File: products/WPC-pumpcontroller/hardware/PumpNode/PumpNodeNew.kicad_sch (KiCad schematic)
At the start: 37 parts, among them J1 Conn_IN, J2 Conn_Coaxial_Small, J3 PWR_CONN, J4 Relay_CONN, K1 Cube_Relay, U1 ULN2003, U13 AMS1117-5.0, U5 ESP32 30 Pin CP2102 Developme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, U7 ISC-SX1262-B, U8 AP2112K-3.3

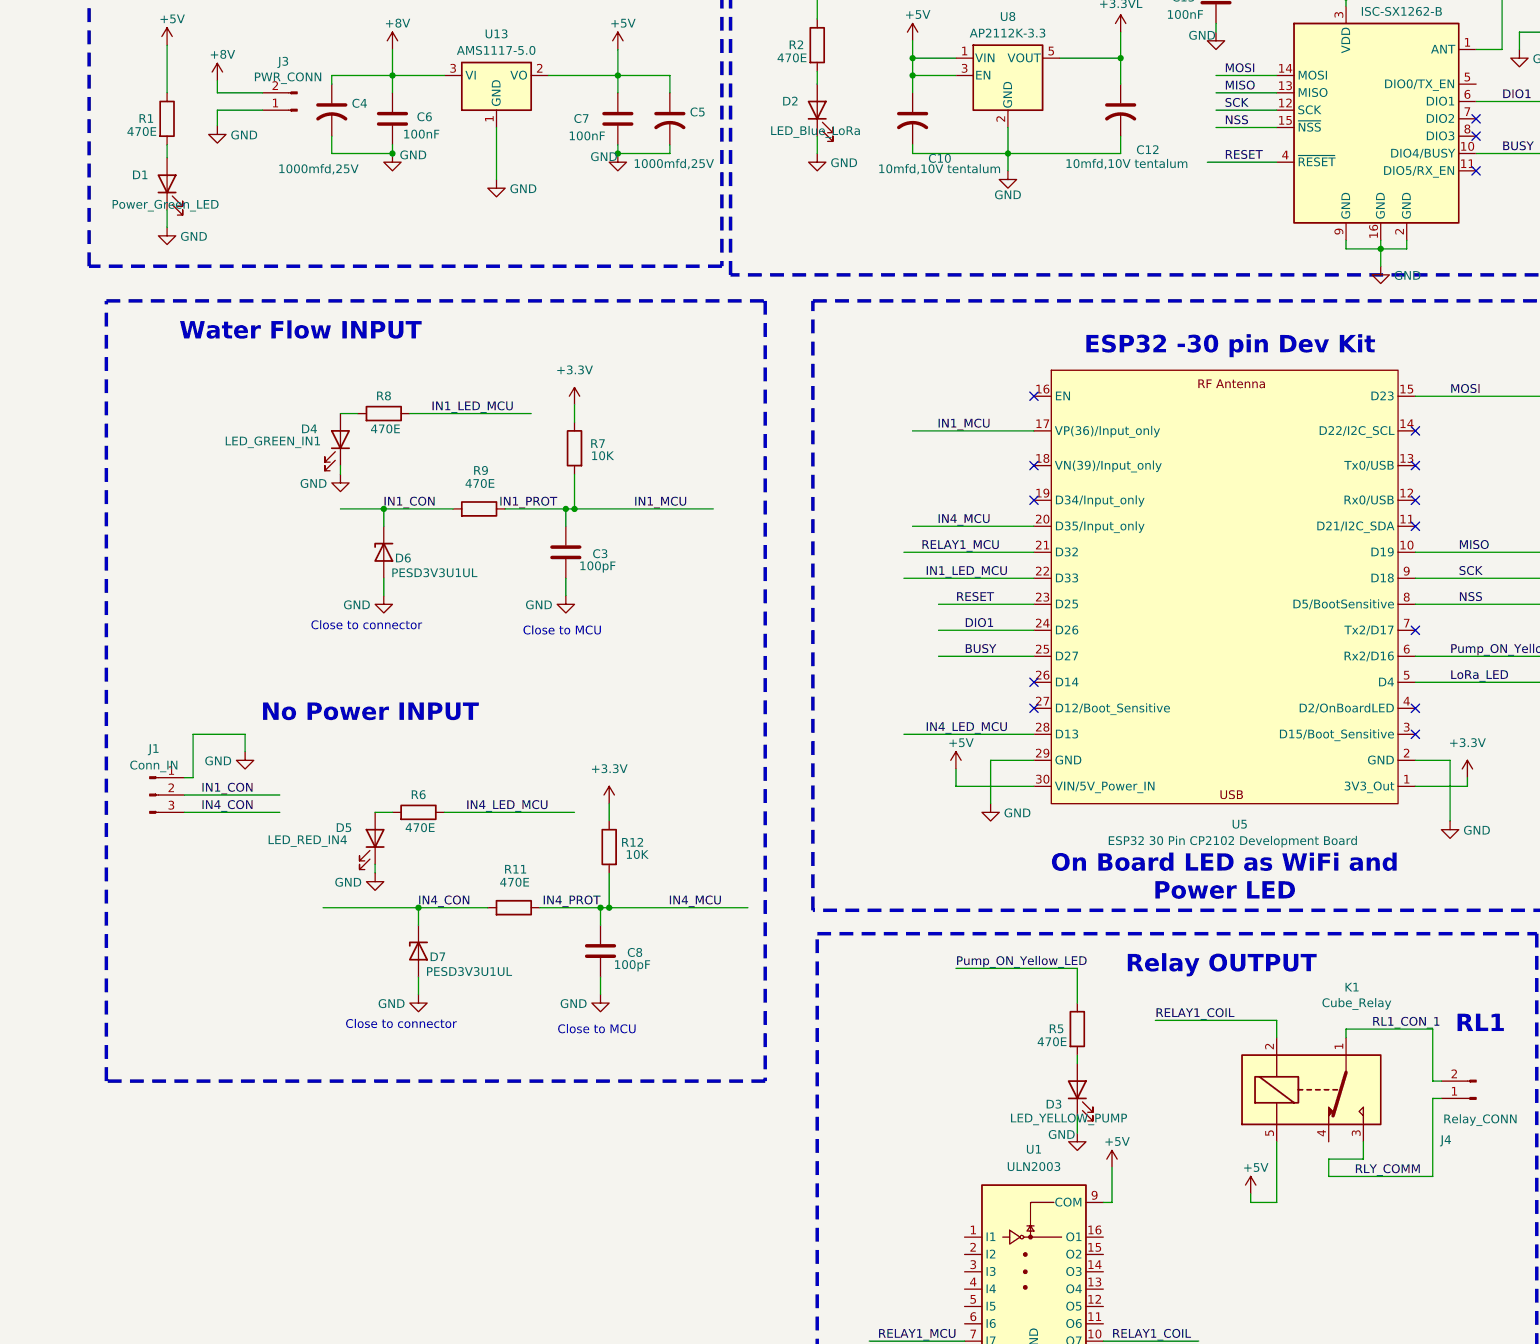
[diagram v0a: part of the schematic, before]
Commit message: WPC: PumpNode + WPC board updates, add 2x panel and Gerber exports
- Update PumpNode and WPC KiCad PCB/schematic/project-local files
- Add WPC-panel2x (2-up panelized PumpNode layout) KiCad project
- Add Gerber/drill export sets for PumpNode and the 2x panel

Co-Authored-By: Claude Sonnet 5 <noreply@anthropic.com>
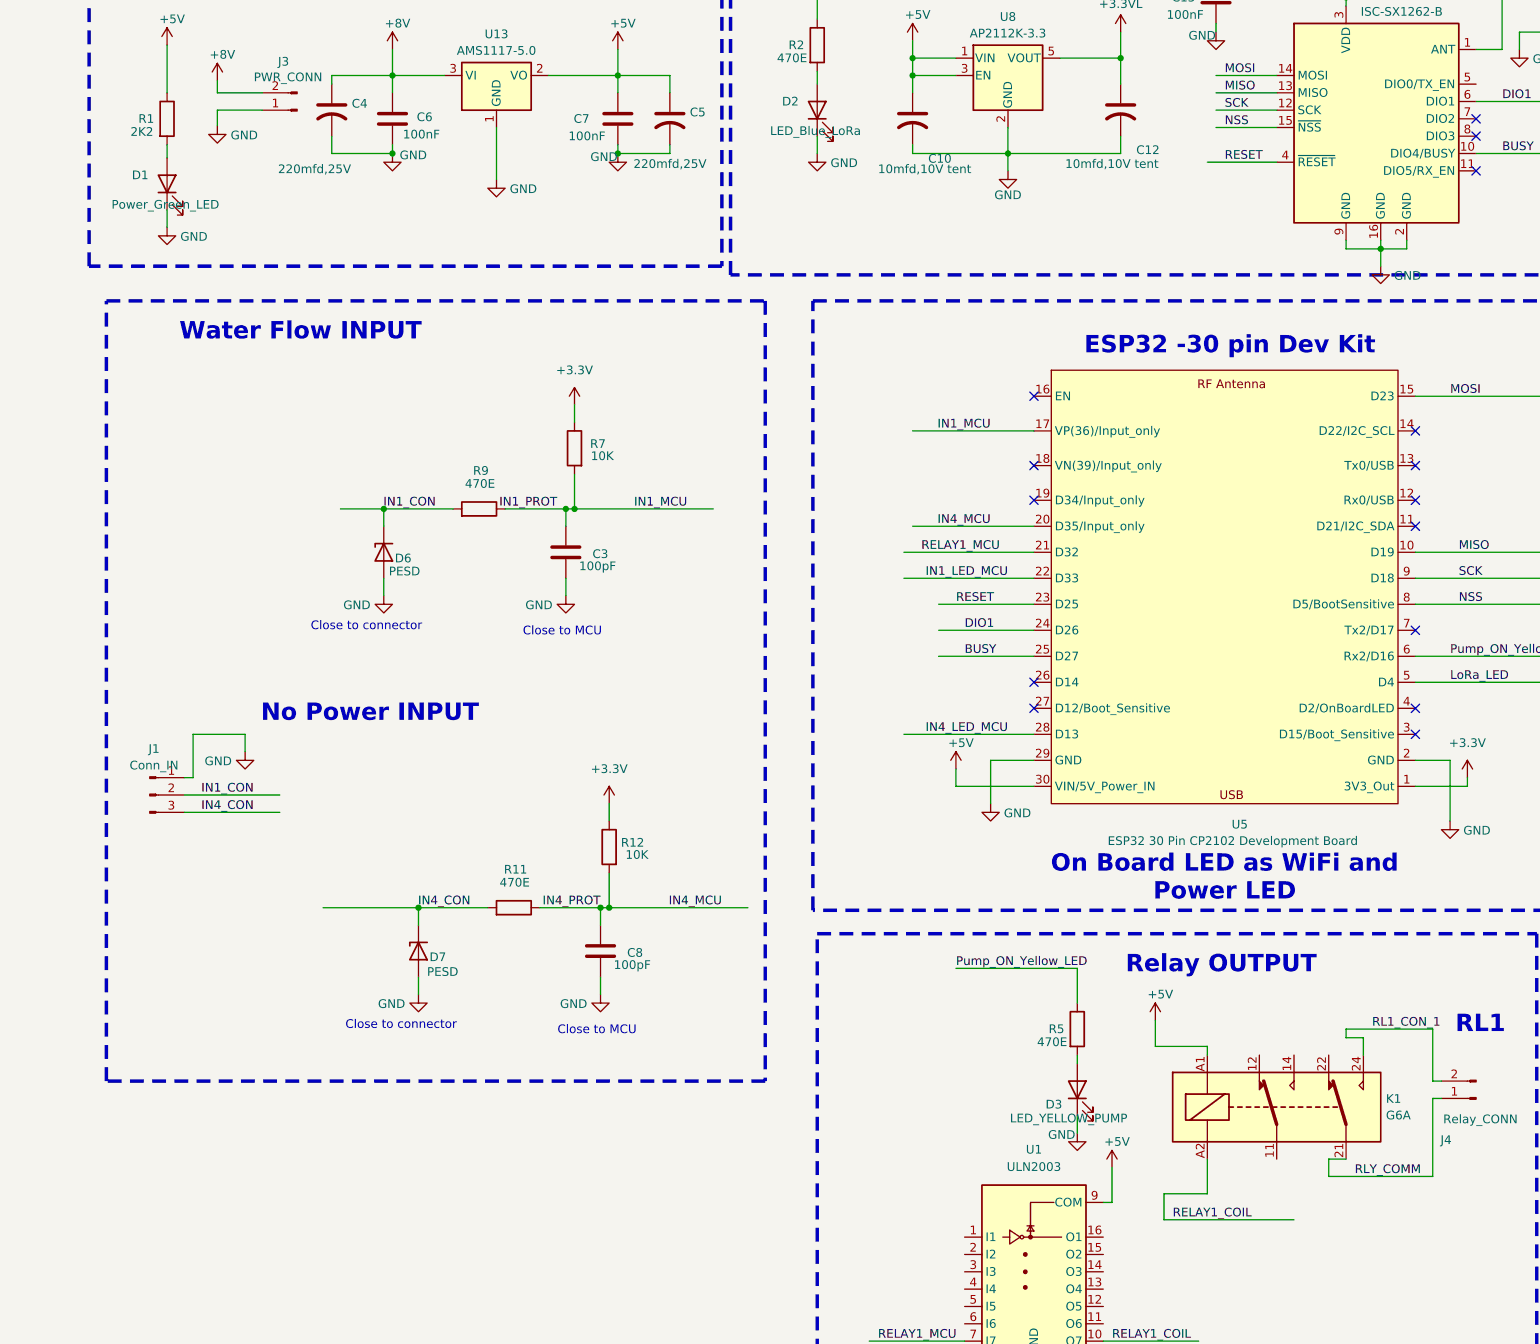
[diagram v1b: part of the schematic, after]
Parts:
- removed D4: LED_GREEN_IN1, LED_SMD:LED_0603_1608Metric, symbol Device:LED
- removed D5: LED_RED_IN4, LED_SMD:LED_0603_1608Metric, symbol Device:LED
- removed K1: Cube_Relay, Relay_THT:Relay_SPDT_SANYOU_SRD_Series_Form_C, symbol Relay:SANYOU_SRD_Form_C
- removed R6, R8: 470E, Resistor_SMD:R_0805_2012Metric, symbol Device:R
- added K1: G6A, Relay_THT:Relay_DPDT_Omron_G6A, symbol Relay:G6A
- C10, C12: value 10mfd,10V tentalum -> 10mfd,10V tent; footprint Capacitor_SMD:C_0603_1608Metric -> Capacitor_SMD:C_0805_2012Metric
- C4, C5: value 1000mfd,25V -> 220mfd,25V
- D6, D7: value PESD3V3U1UL -> PESD; footprint Diode_SMD:D_SOD-882 -> Diode_SMD:D_0805_2012Metric
- J1: footprint Connector_Phoenix_MSTB:PhoenixContact_MSTBA_2,5_3-G-5,08_1x03_P5.08mm_Horizontal -> TerminalBlock_MetzConnect:TerminalBlock_MetzConnect_Type086_RT03403HBLC_1x03_P3.81mm_Horizontal
- J3, J4: footprint PhoenixContact_MSTBA_2,5_2-G-5,08_1x02_P5.08mm_Horizontal -> TerminalBlock_MetzConnect:TerminalBlock_MetzConnect_Type086_RT03402HBLC_1x02_P3.81mm_Horizontal
- R1: value 470E -> 2K2
- U1: footprint Package_SO:SOIC-16W_5.3x10.2mm_P1.27mm -> Package_SO:SOIC-16_3.9x9.9mm_P1.27mm
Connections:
- net +5V: now also K1.A1
- net RELAY1_COIL: now also K1.A2
- net RL1_CON_1: now also K1.24
- net RLY_COMM: now also K1.21
